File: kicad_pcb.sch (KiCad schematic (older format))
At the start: 160 parts, among them J1 USB_B_Mini, SW1 SW_Push, U1 ATmega32U4-AU, Y1 Resonator_Small

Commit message: rerouted the bottom row
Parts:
- added D23, D38, D66, D69: D_Small, Diode_SMD:D_0805_2012Metric, symbol Device:D_Small
- added MX23: R ALT, MX_Alps_Hybrid:MX-2U-NoLED, symbol MX_Alps_Hybrids:MX-1U
- added MX38: R WIN, MX_Alps_Hybrid:MX-1.25U-NoLED, symbol MX_Alps_Hybrids:MX-1U
- added MX62-1: CTRL, MX_Alps_Hybrid:MX-1.5U-NoLED, symbol MX_Alps_Hybrids:MX-1U
- added MX63-1: WIN, MX_Alps_Hybrid:MX-1.25U-NoLED, symbol MX_Alps_Hybrids:MX-1U
- added MX64-1: ALT, MX_Alps_Hybrid:MX-1.5U-NoLED, symbol MX_Alps_Hybrids:MX-1U
- added MX65-1: L SPACE, MX_Alps_Hybrid:MX-2.75U-ReversedStabilizers-NoLED, symbol MX_Alps_Hybrids:MX-1U
- added MX66: R ALT, MX_Alps_Hybrid:MX-1.5U-NoLED, symbol MX_Alps_Hybrids:MX-1U
- added MX69: R CTRL, MX_Alps_Hybrid:MX-2.25U-NoLED, symbol MX_Alps_Hybrids:MX-1U
- added MX70-1: R SPACE, MX_Alps_Hybrid:MX-2.75U-NoLED, symbol MX_Alps_Hybrids:MX-1U
- MX61: footprint MX_Alps_Hybrid:MXOnly-1U-NoLED -> MX_Alps_Hybrid:MX-1U-NoLED
- MX62, MX63, MX64: footprint MX_Alps_Hybrid:MXOnly-1.25U-NoLED -> MX_Alps_Hybrid:MX-1.25U-NoLED
- MX65: value LEFT SPACE -> L SPACE; footprint MX_Alps_Hybrid:MXOnly-2.25U-ReversedStabilizers-NoLED -> MX_Alps_Hybrid:MX-2.25U-ReversedStabilizers-NoLED
- MX70: value RIGHT SPACE -> R SPACE
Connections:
- net COL1: now also MX62-1.1 (COL)
- net COL2: now also MX63-1.1 (COL)
- net COL3: now also MX64-1.1 (COL)
- net COL4: now also MX65-1.2 (ROW)
- net COL5: now also MX66.1 (COL)
- net COL7: now also MX23.1 (COL), MX38.2 (ROW)
- net COL8: now also MX69.1 (COL)
- net COL9: now also MX70-1.1 (COL)
- net ROW1: now also D23.1 (K)
- net ROW2: now also D38.1 (K)
- net ROW4: now also D66.1 (K), D69.1 (K)
- net at D70.2 (A), MX70.2 (ROW): now also MX70-1.2 (ROW)
- net at D65.2 (A), MX65.2 (ROW): now also MX65-1.1 (COL)
- net at D64.2 (A), MX64.2 (ROW): now also MX64-1.2 (ROW)
- net at D63.2 (A), MX63.2 (ROW): now also MX63-1.2 (ROW)
- net at D62.2 (A), MX62.2 (ROW): now also MX62-1.2 (ROW)
- new net: D69.2 (A), MX69.2 (ROW)
- new net: D38.2 (A), MX38.1 (COL)
- new net: D66.2 (A), MX66.2 (ROW)
- new net: D23.2 (A), MX23.2 (ROW)

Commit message: tidied up some overlapping pads
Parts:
- MX65: value L SPACE -> L SPACE (2.25u)
- MX65-1: value L SPACE -> L SPACE (2.75u); footprint MX_Alps_Hybrid:MX-2.75U-ReversedStabilizers-NoLED -> MX_Alps_Hybrid:MX-2.75U-NoLED
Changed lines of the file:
@@
 P 8575 6075
 F 0 "MX65" H 8661 6292 60  0000 C CNN
-F 1 "L SPACE" H 8661 6218 20  0000 C CNN
+F 1 "L SPACE (2.25u)" H 8661 6218 20  0000 C CNN
 F 2 "MX_Alps_Hybrid:MX-2.25U-ReversedStabilizers-NoLED" H 8550 6050 60  0001 C CNN
 F 3 "" H 8550 6050 60  0001 C CNN
@@
 P 8100 6075
 F 0 "MX65-1" H 8186 6292 60  0000 C CNN
-F 1 "L SPACE" H 8186 6218 20  0000 C CNN
-F 2 "MX_Alps_Hybrid:MX-2.75U-ReversedStabilizers-NoLED" H 8075 6050 60  0001 C CNN
+F 1 "L SPACE (2.75u)" H 8186 6218 20  0000 C CNN
+F 2 "MX_Alps_Hybrid:MX-2.75U-NoLED" H 8075 6050 60  0001 C CNN
 F 3 "" H 8075 6050 60  0001 C CNN
 	1    8100 6075

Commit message: Introduced mx and alps footprints for every switch
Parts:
- added MX30-2: BACKSPACE (2u), MX_Alps_Hybrid:MX-2U-NoLED, symbol MX_Alps_Hybrids:MX-1U
- MX1, MX10, MX11, MX12, MX13, MX14, MX15, MX17, MX18, MX19, MX2, MX20, MX21, MX22, MX24, MX25, MX26, MX27, MX28, MX29, MX3, MX31, MX32, MX33, MX34, MX35, MX36, MX37, MX39, MX4, MX40, MX41, MX42, MX43, MX44, MX45, MX46, MX47, MX48, MX49, MX5, MX50, MX51, MX52, MX53, MX54, MX55, MX56, MX57, MX58, MX59, MX6, MX60, MX68, MX7, MX71, MX72, MX73, MX74, MX75, MX8, MX9: footprint MX_Alps_Hybrid:MXOnly-1U-NoLED -> MX_Alps_Hybrid:MX-1U-NoLED
- MX16: renamed from MX16-1; footprint MX_Alps_Hybrid:MXOnly-1.5U-NoLED -> MX_Alps_Hybrid:MX-1.5U-NoLED
- MX16-1: renamed from MX16; footprint MX_Alps_Hybrid:MXOnly-1U-NoLED -> MX_Alps_Hybrid:MX-1U-NoLED
- MX30: renamed from MX30-1; footprint MX_Alps_Hybrid:MXOnly-1.5U-NoLED -> MX_Alps_Hybrid:MX-1.5U-NoLED
- MX30-1: renamed from MX30; footprint MX_Alps_Hybrid:MXOnly-1U-NoLED -> MX_Alps_Hybrid:MX-1U-NoLED
- MX31-1, MX37-1, MX39-1, MX45-1: footprint MX_Alps_Hybrid:MXOnly-1.25U-NoLED -> MX_Alps_Hybrid:MX-1.25U-NoLED
- MX70: footprint MX_Alps_Hybrid:MXOnly-2U-ReversedStabilizers-NoLED -> MX_Alps_Hybrid:MX-2U-ReversedStabilizers-NoLED
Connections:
- net COL0: now also MX16.2 (ROW); no longer MX16.1 (COL)
- net COL14: now also MX30-1.2 (ROW), MX30-2.1 (COL); no longer MX30-1.1 (COL)
- net at D16.2 (A), MX16-1.2 (ROW): now also MX16.1 (COL); no longer MX16.2 (ROW)
- net at D30.2 (A), MX30.2 (ROW): now also MX30-1.1 (COL), MX30-2.2 (ROW); no longer MX30-1.2 (ROW)
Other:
- moved on the sheet: MX16, MX30-1

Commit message: Added symmetric 7u bottom row
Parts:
- added MX38-2: R WIN (1u), MX_Alps_Hybrid:MX-1U-NoLED, symbol MX_Alps_Hybrids:MX-1U
- added MX6-2: CENTER (7u), MX_Alps_Hybrid:MX-7U-ReversedStabilizers-NoLED, symbol MX_Alps_Hybrids:MX-1U
- added MX63-2: WIN (1u), MX_Alps_Hybrid:MX-1U-NoLED, symbol MX_Alps_Hybrids:MX-1U
- added MX64-2: ALT (1.5u), MX_Alps_Hybrid:MX-1.5U-NoLED, symbol MX_Alps_Hybrids:MX-1U
- added MX69-2: R CTRL (1.5u), MX_Alps_Hybrid:MX-1.5U-NoLED, symbol MX_Alps_Hybrids:MX-1U
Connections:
- net COL2: now also MX63-2.1 (COL)
- net COL3: now also MX64-2.1 (COL)
- net COL7: now also MX38-2.1 (COL), MX6-2.1 (COL)
- net COL8: now also MX69-2.2 (ROW)
- net at D68.2 (A), MX68.2 (ROW): now also MX6-2.2 (ROW)
- net at D64.2 (A), MX64-1.2 (ROW), MX64.2 (ROW): now also MX64-2.2 (ROW)
- net at D63.2 (A), MX63-1.2 (ROW), MX63.2 (ROW): now also MX63-2.2 (ROW)
- net at D69.2 (A), MX69.2 (ROW): now also MX69-2.1 (COL)
- net at D38.2 (A), MX38.1 (COL): now also MX38-2.2 (ROW)
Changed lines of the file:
@@
 Connection ~ 11250 2050
 Wire Wire Line
-	12500 5050 12500 6050
+	12500 5050 12500 5650
 Connection ~ 12500 5050
 Connection ~ 12500 2050
@@
 	5775 6050 5900 6050
 Wire Wire Line
-	5900 6050 5900 5650
-Wire Wire Line
 	5900 5650 6250 5650
 Connection ~ 6250 5650
@@
 	7025 6050 7150 6050
 Wire Wire Line
-	7150 6050 7150 5650
+	7150 6050 7150 5750
 Wire Wire Line
 	7150 5650 7500 5650
@@
 $EndComp
 Wire Wire Line
-	13750 6050 13750 5050
+	13750 6050 13750 5650
 Connection ~ 13750 5050
 Connection ~ 10000 5050
@@
 Wire Wire Line
 	10750 3450 12000 3450
-Wire Wire Line
-	12500 2050 12500 3050
 $Comp
 L MX_Alps_Hybrids:MX-1U MX23
@@
 	10000 5050 10000 6050
 Wire Wire Line
-	12500 3050 12500 4050
+	12500 3050 12500 3800
 Wire Wire Line
 	12325 4050 12500 4050
@@
 Wire Wire Line
 	21250 3050 21250 3800
+$Comp
+L MX_Alps_Hybrids:MX-1U MX63-2
+U 1 1 5E31230E
+P 5350 5775
+F 0 "MX63-2" H 5436 5992 60  0000 C CNN
+F 1 "WIN (1u)" H 5436 5918 20  0000 C CNN
+F 2 "MX_Alps_Hybrid:MX-1U-NoLED" H 5325 5750 60  0001 C CNN
+F 3 "" H 5325 5750 60  0001 C CNN
+	1    5350 5775
+	1    0    0    -1
+$EndComp
+Wire Wire Line
+	5525 5750 5900 5750
+Wire Wire Line
+	5900 5650 5900 5750
+Connection ~ 5900 5750
+Wire Wire Line
+	5900 5750 5900 6050
+Wire Wire Line
+	5325 5950 5325 6250
+Wire Wire Line
+	5325 6250 5575 6250
+Connection ~ 5575 6250
+$Comp
+L MX_Alps_Hybrids:MX-1U MX64-2
+U 1 1 5E3613CF
+P 6600 5775
+F 0 "MX64-2" H 6686 5992 60  0000 C CNN
+F 1 "ALT (1.5u)" H 6686 5918 20  0000 C CNN
+F 2 "MX_Alps_Hybrid:MX-1.5U-NoLED" H 6575 5750 60  0001 C CNN
+F 3 "" H 6575 5750 60  0001 C CNN
+	1    6600 5775
+	1    0    0    -1
+$EndComp
+Wire Wire Line
+	6775 5750 7150 5750
+Connection ~ 7150 5750
+Wire Wire Line
+	7150 5750 7150 5650
+Wire Wire Line
+	6575 5950 6575 6250
+Wire Wire Line
+	6575 6250 6825 6250
+Connection ~ 6825 6250
+$Comp
+L MX_Alps_Hybrids:MX-1U MX6-2
+U 1 1 5E3B1C21
+P 11850 6075
+F 0 "MX6-2" H 11936 6292 60  0000 C CNN
+F 1 "CENTER (7u)" H 11936 6218 20  0000 C CNN
+F 2 "MX_Alps_Hybrid:MX-7U-ReversedStabilizers-NoLED" H 11825 6050 60  0001 C CNN
+F 3 "" H 11825 6050 60  0001 C CNN
+	1    11850 6075
+	1    0    0    -1
+$EndComp
+Wire Wire Line
+	11825 6250 12000 6250
+Connection ~ 12000 6250
+Wire Wire Line
+	12025 6050 12150 6050
+Wire Wire Line
+	12150 6050 12150 5650
+Wire Wire Line
+	12150 5650 12500 5650
+Connection ~ 12500 5650
+Wire Wire Line
+	12500 5650 12500 6050
+$Comp
+L MX_Alps_Hybrids:MX-1U MX38-2
+U 1 1 5E4599AF
+P 11850 3825
+F 0 "MX38-2" H 11936 4042 60  0000 C CNN
+F 1 "R WIN (1u)" H 11936 3968 20  0000 C CNN
+F 2 "MX_Alps_Hybrid:MX-1U-NoLED" H 11825 3800 60  0001 C CNN
+F 3 "" H 11825 3800 60  0001 C CNN
+	1    11850 3825
+	1    0    0    -1
+$EndComp
+Wire Wire Line
+	12025 3800 12500 3800
+Connection ~ 12500 3800
+Wire Wire Line
+	12500 3800 12500 4050
+Wire Wire Line
+	11825 4000 11825 4250
+Wire Wire Line
+	11825 4250 12000 4250
+Connection ~ 12000 4250
+$Comp
+L MX_Alps_Hybrids:MX-1U MX69-2
+U 1 1 5E4AF83D
+P 13100 6075
+F 0 "MX69-2" H 13186 6292 60  0000 C CNN
+F 1 "R CTRL (1.5u)" H 13186 6218 20  0000 C CNN
+F 2 "MX_Alps_Hybrid:MX-1.5U-NoLED" H 13075 6050 60  0001 C CNN
+F 3 "" H 13075 6050 60  0001 C CNN
+	1    13100 6075
+	-1   0    0    1
+$EndComp
+Wire Wire Line
+	13125 5900 13400 5900
+Wire Wire Line
+	13400 5900 13400 5650
+Wire Wire Line
+	13400 5650 13750 5650
+Connection ~ 13750 5650
+Wire Wire Line
+	13750 5650 13750 5050
+Connection ~ 13250 6250
+Wire Wire Line
+	12925 6250 13250 6250
+Wire Wire Line
+	12925 6100 12925 6250
+Wire Wire Line
+	12500 2050 12500 3050
 $EndSCHEMATC

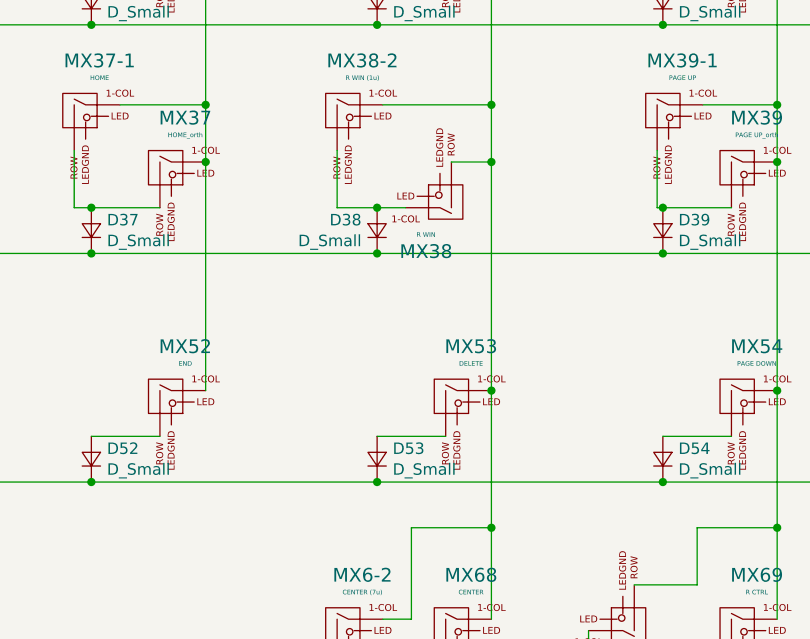
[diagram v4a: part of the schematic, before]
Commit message: created additional space around the stabilisers to prevent shorting
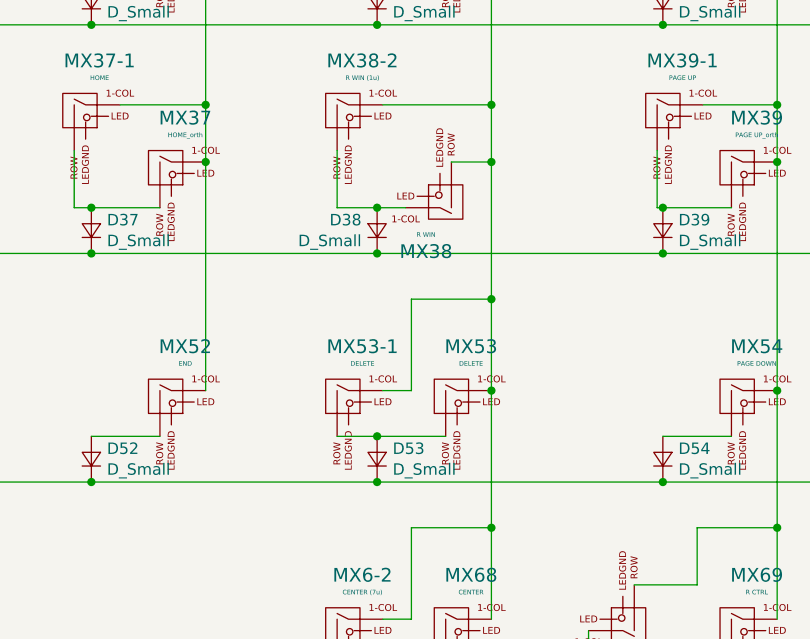
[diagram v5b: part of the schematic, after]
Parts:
- added MX53-1: DELETE, MX_Alps_Hybrid:MX-2.75U-ReversedStabilizers-NoLED, symbol MX_Alps_Hybrids:MX-1U
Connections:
- net COL7: now also MX53-1.1 (COL)
- net at D53.2 (A), MX53.2 (ROW): now also MX53-1.2 (ROW)
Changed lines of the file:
@@
 Connection ~ 12500 4050
 Wire Wire Line
-	12500 4050 12500 5050
+	12500 4050 12500 4650
 $Comp
 L MX_Alps_Hybrids:MX-1U MX30-2
@@
 Wire Wire Line
 	12500 2050 12500 3050
+$Comp
+L MX_Alps_Hybrids:MX-1U MX53-1
+U 1 1 5D5420BE
+P 11850 5075
+F 0 "MX53-1" H 11936 5292 60  0000 C CNN
+F 1 "DELETE" H 11936 5218 20  0000 C CNN
+F 2 "MX_Alps_Hybrid:MX-2.75U-ReversedStabilizers-NoLED" H 11825 5050 60  0001 C CNN
+F 3 "" H 11825 5050 60  0001 C CNN
+	1    11850 5075
+	1    0    0    -1
+$EndComp
+Wire Wire Line
+	12025 5050 12150 5050
+Wire Wire Line
+	12150 5050 12150 4650
+Wire Wire Line
+	12150 4650 12500 4650
+Connection ~ 12500 4650
+Wire Wire Line
+	12500 4650 12500 5050
+Wire Wire Line
+	11825 5250 12000 5250
+Connection ~ 12000 5250
 $EndSCHEMATC
